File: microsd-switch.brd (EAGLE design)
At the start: 34.8 x 48.2 mm, 12 parts, among them IC1 SN74CBT3257D, IC2 SN74CBT3257D, U1 USD-SOCKETNEW

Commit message: Revert "MicroSD Switch Rev Alpha released"
This reverts commit e0d3fcd5b1a8d34c9a3cecba9fd5e98c93932393.
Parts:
- moved JP3 58.0 mm to (81.3, 77.5), turned to 180 degrees
- moved R1 45.7 mm to (40.1, 67.6), turned to 180 degrees
- moved LED2 32.5 mm to (41.7, 60.5), turned to 180 degrees
- moved JP1 32.1 mm to (77.5, 41.9)
- moved R4 29.9 mm to (37.1, 59.9), turned to 270 degrees
- moved U1 24.3 mm to (67.3, 58.4), flipped to the top
- moved JP2 23.3 mm to (36.8, 40.6), turned to 0 degrees
- moved R3 16.8 mm to (37.1, 53.3), turned to 270 degrees
- moved IC1 14.3 mm to (59.2, 52.1)
- moved LED1 13.1 mm to (41.7, 53.8), turned to 180 degrees
- moved R2 11.3 mm to (40.1, 75.2)
- moved IC2 10.1 mm to (52.6, 66.8)
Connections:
- net CLK-Y renamed N$1
- net CLK-A: now also JP2.3; no longer JP2.4
- net CLK-B: now also JP3.3; no longer JP3.4
- net GND: now also JP2.5, JP3.5; no longer JP2.3, JP3.3
- net VDD-A: now also JP2.4; no longer JP2.5
- net VDD-B: now also JP3.4; no longer JP3.5
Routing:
- net GND: track 61.4 -> 191.6 mm, vias 8 -> 1
- net OE: track 94.8 -> 30.6 mm, vias 5 -> 2
- net DAT0-B: track 22.1 -> 48.2 mm, vias 1 -> 0
- net DAT2-A: track 19.1 -> 44.8 mm, vias 0 -> 1
- net DAT1-B: track 26.2 -> 43.9 mm
- net N$2: track 12.9 -> 30.5 mm, vias 1 -> 2
- net DAT1-Y: track 19.2 -> 35.2 mm, vias 1 -> 0
- net VCC: track 53.6 -> 67.8 mm, vias 7 -> 2
- net DAT2-B: track 24.6 -> 11.5 mm, vias 1 -> 0
- net CLK-A: track 20.7 -> 33.1 mm
- net DAT1-A: track 19.8 -> 30.9 mm
- net DAT0-Y: track 19.4 -> 30.4 mm, vias 3 -> 0
- net DAT3-A: track 20.2 -> 31.1 mm
- net CLK-B: track 26.9 -> 36.7 mm, vias 1 -> 0
- net HOSTSELECT: track 68.9 -> 59.3 mm, vias 3 -> 2
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- removed copper zone on layer 16, net GND
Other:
- board size 34.8 x 48.2 mm -> 49.2 x 41.9 mm
- board text added: "MicroSD Switcher by Joel Fernandes"
- board text removed: "CC BY-NC-SA 3.0"
- board text removed: "MicroSD Switcher Alpha"
- board text removed: "by Joel Fernandes"

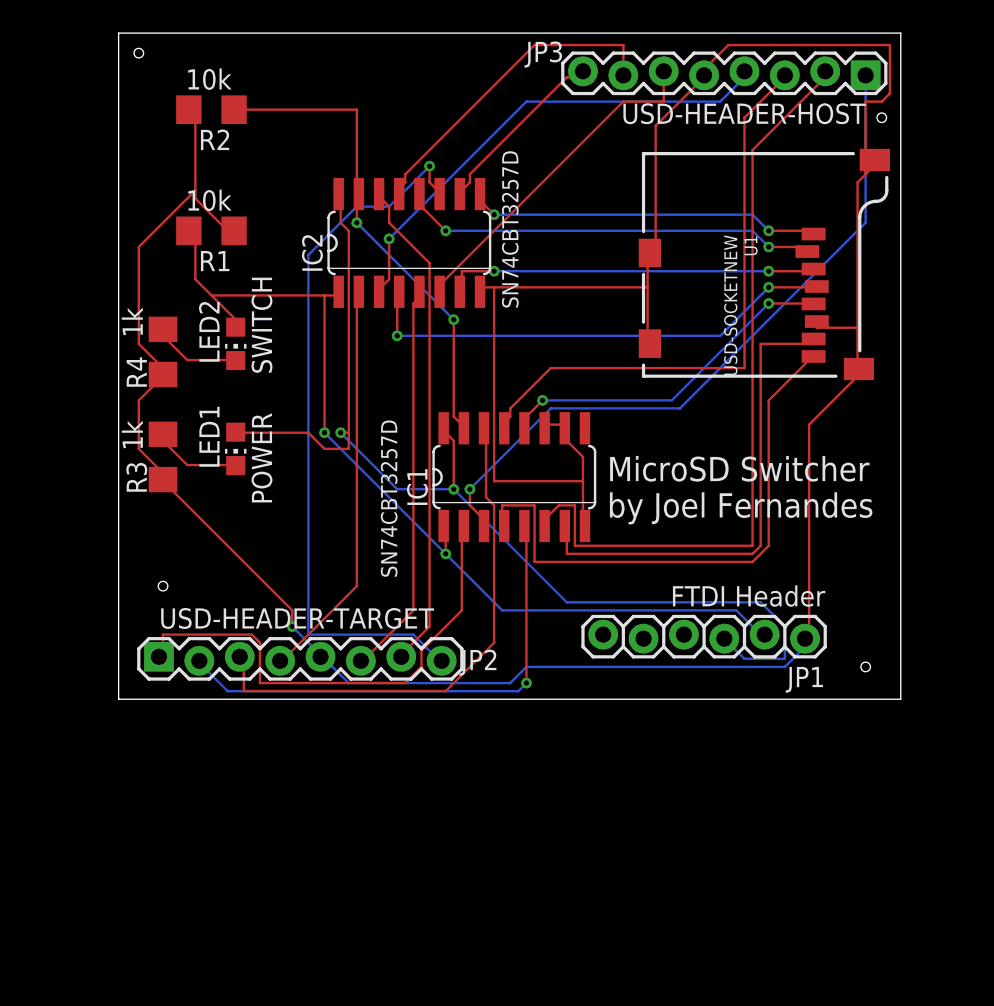
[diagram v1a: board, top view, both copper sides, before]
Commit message: Reduced uSD header connector size.
Signed-off-by: Joel Fernandes <joelf@ti.com>
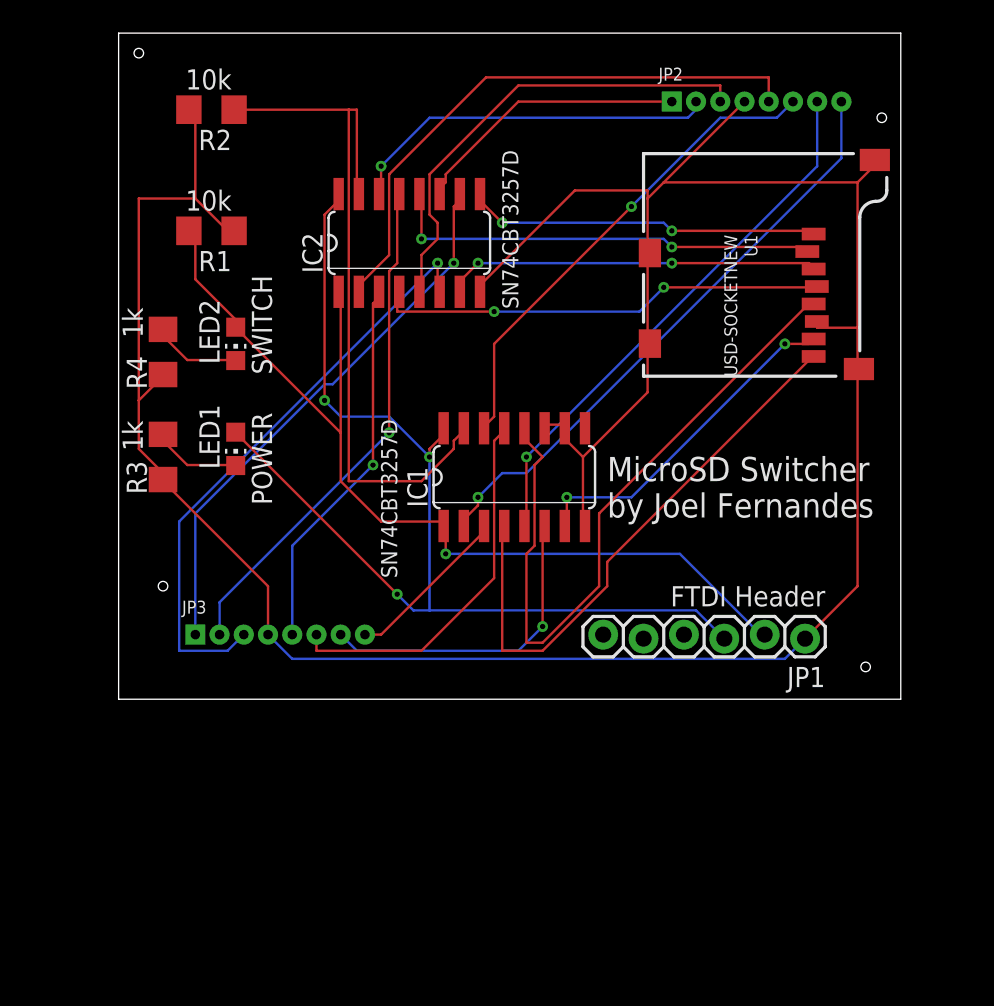
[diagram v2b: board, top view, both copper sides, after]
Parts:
- JP2: value USD-HEADER-TARGET -> SD_HEADER_TARGET; device SparkFun:1X08_LOCK -> joels-parts:1X08_SMALL
- JP3: value USD-HEADER-HOST -> SD_HEADER_HOST; device SparkFun:1X08_LOCK -> joels-parts:1X08_SMALL
- moved JP2 51.2 mm to (74.2, 75.7)
- moved JP3 51.2 mm to (44.2, 42.2), turned to 0 degrees
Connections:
- net CLK-A: now also JP2.6; no longer JP2.3
- net CLK-B: now also JP3.6; no longer JP3.3
- net CMD-A: now also JP2.3; no longer JP2.6
- net CMD-B: now also JP3.3; no longer JP3.6
- net DAT0-A: now also JP2.7; no longer JP2.2
- net DAT0-B: now also JP3.7; no longer JP3.2
- net DAT1-A: now also JP2.8; no longer JP2.1
- net DAT1-B: now also JP3.8; no longer JP3.1
- net DAT2-A: now also JP2.1; no longer JP2.8
- net DAT2-B: now also JP3.1; no longer JP3.8
- net DAT3-A: now also JP2.2; no longer JP2.7
- net DAT3-B: now also JP3.2; no longer JP3.7
- net GND: now also JP2.4, JP3.4; no longer JP2.5, JP3.5
- net VDD-A: now also JP2.5; no longer JP2.4
- net VDD-B: now also JP3.5; no longer JP3.4
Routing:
- net DAT1-B: track 43.9 -> 10.6 mm, vias 1 -> 0
- net DAT0-B: track 48.2 -> 20.1 mm, vias 0 -> 1
- net DAT2-A: track 44.8 -> 17.6 mm, vias 1 -> 0
- net DAT2-B: track 11.5 -> 35.0 mm, vias 0 -> 1
- net N$1: track 21.8 -> 43.9 mm, vias 2 -> 0
- net CMD-B: track 21.3 -> 37.4 mm, vias 0 -> 1
- net OE: track 30.6 -> 45.4 mm, vias 2 -> 0
- net GND: track 191.6 -> 177.4 mm, vias 1 -> 0
- net CLK-B: track 36.7 -> 23.7 mm
- net DAT3-B: track 20.5 -> 32.4 mm, vias 0 -> 1
- net VDD-A: track 25.3 -> 36.2 mm
- net DAT0-Y: track 30.4 -> 21.5 mm, vias 0 -> 2
- net DAT3-A: track 31.1 -> 23.6 mm, vias 0 -> 1
- net DAT1-A: track 30.9 -> 37.5 mm, vias 0 -> 1
- net VDD-B: track 30.5 -> 23.9 mm
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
